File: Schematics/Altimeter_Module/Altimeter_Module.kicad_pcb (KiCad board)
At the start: 4 copper layers, 69.5 x 60 mm, 104 parts, among them J1 Stack Male Edge Connector, J2 Main E-Match, J3 Drogue E-Match, J4 USB_B_Micro, J5 SWD_01x04_Pin, Q1 AO3400A, Q2 AO4406AL, Q3 AO3400A, Q4 AO3400A, Q5 AO4406AL, SW1 SW_STM_RESET, SW2 SW_STM_BOOT_MODE, U1 KX134-1211, U10 ACS70331EOLC, U12 AMS1117-3.3, U2 MS560702BA03-50, U3 W25Q128JVS, U4 LM66100DCKR, U5 LM66100DCKR, U6 STM32F103CBT6, U7 LM66100DCKR, U8 ISO1042BDWVR, U9 MPU-6050, Y1 X322516MMB4SI

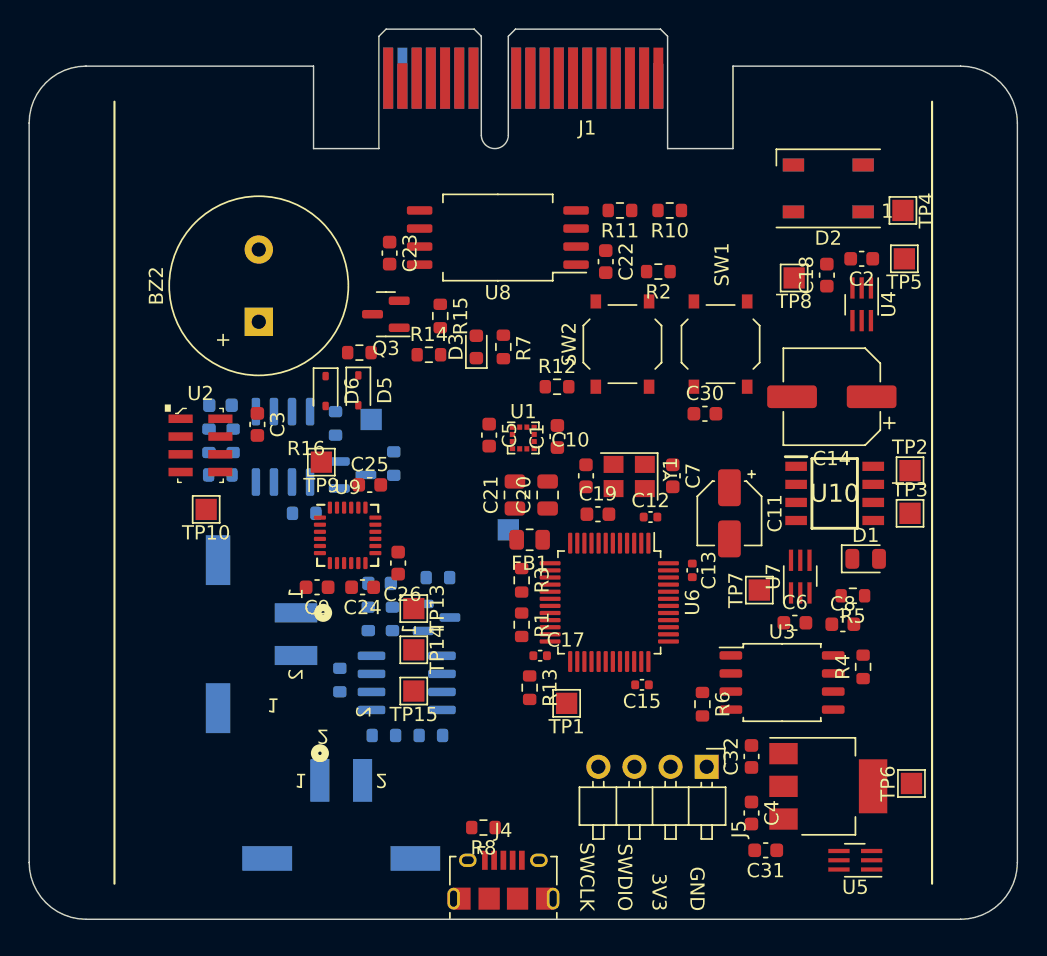
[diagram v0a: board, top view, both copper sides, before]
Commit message: Reset PCB layout
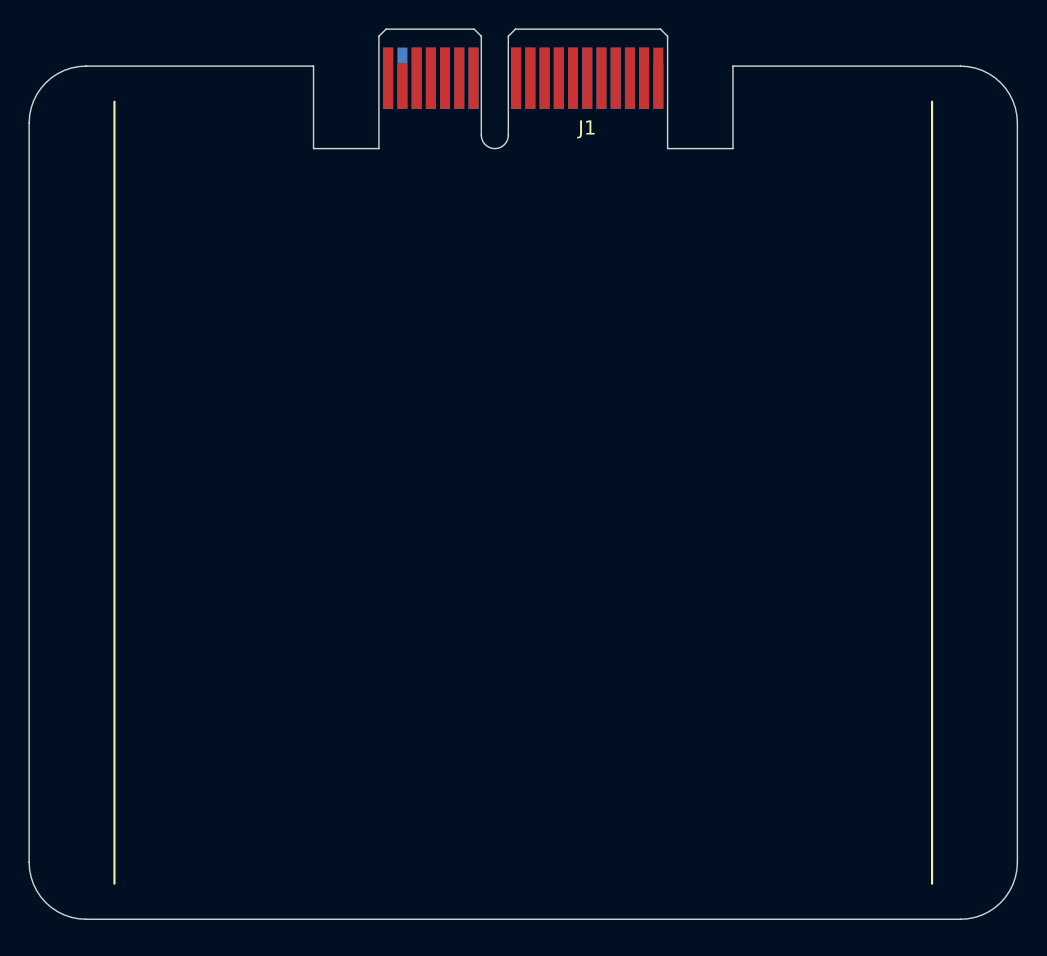
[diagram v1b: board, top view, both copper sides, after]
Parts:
- removed BZ2: PKM13EPYH4000, footprints:Buzzer_12.6x9.5RM5.0
- removed C1, C24, C3, C30, C5, C8, C9: 100nF, Capacitor_SMD:C_0603_1608Metric
- removed C10, C7: 10p, Capacitor_SMD:C_0603_1608Metric
- removed C11: 10uF, Capacitor_SMD:CP_Elec_4x5.4
- removed C12, C13, C15, C17: 100n, Capacitor_SMD:C_0402_1005Metric
- removed C14: 100uF, Capacitor_SMD:CP_Elec_6.3x5.9
- removed C18: 0.1uF, Capacitor_SMD:C_0603_1608Metric
- removed C19: 10n, Capacitor_SMD:C_0603_1608Metric
- removed C2, C4, C6: 1uF, Capacitor_SMD:C_0603_1608Metric
- removed C20, C21: 1uF, Capacitor_SMD:C_0805_2012Metric
- removed C22, C23: 0.1u, Capacitor_SMD:C_0603_1608Metric
- removed C25: 2.2nF, Capacitor_SMD:C_0603_1608Metric
- removed C26: 10nF, Capacitor_SMD:C_0603_1608Metric
- removed C31, C32: 10uF, Capacitor_SMD:C_0603_1608Metric
- removed D1: PWR_LED (GRN), LED_SMD:LED_0805_2012Metric
- removed D2, D4: WS2812B, LED_SMD:LED_WS2812B_PLCC4_5.0x5.0mm_P3.2mm
- removed D3: DB_LED (YLW), LED_SMD:LED_0603_1608Metric
- removed D5, D6: 1N5819WS, Diode_SMD:D_SOD-323
- removed D7: FIRE_MAIN (RED), LED_SMD:LED_0603_1608Metric
- removed D8: FIRE_DRGE (RED), LED_SMD:LED_0603_1608Metric
- removed FB1: 100R, Resistor_SMD:R_0805_2012Metric
- removed J2: Main E-Match, footprints:CONN_2-1445057-2_TYCO
- removed J3: Drogue E-Match, footprints:CONN_2-1445057-2_TYCO
- removed J4: USB_B_Micro, footprints:USB_Micro-B_Amphenol_10118194_Horizontal
- removed J5: SWD_01x04_Pin, SWD_Header:SWD_PinHeader_1x04_P2.54mm_Horizontal
- removed Q1, Q3, Q4: AO3400A, Package_TO_SOT_SMD:SOT-23
- removed Q2, Q5: AO4406AL, Package_SO:SOIC-8_3.9x4.9mm_P1.27mm
- removed R1, R3: 4.7k, Resistor_SMD:R_0603_1608Metric
- removed R10: 30k, Resistor_SMD:R_0603_1608Metric
- removed R11, R15, R19, R2, R25, R4, R6: 10k, Resistor_SMD:R_0603_1608Metric
- removed R12, R13, R17, R21, R22, R23: 100k, Resistor_SMD:R_0603_1608Metric
- removed R14, R18, R20, R24, R26, R27, R9: 510R, Resistor_SMD:R_0603_1608Metric
- removed R16: 1k, Resistor_SMD:R_0603_1608Metric
- removed R5: 820R, Resistor_SMD:R_0603_1608Metric
- removed R7: 560R, Resistor_SMD:R_0603_1608Metric
- removed R8: 1.5k, Resistor_SMD:R_0603_1608Metric
- removed SW1: SW_STM_RESET, Button_Switch_SMD:SW_Push_1P1T_XKB_TS-1187A
- removed SW2: SW_STM_BOOT_MODE, Button_Switch_SMD:SW_Push_1P1T_XKB_TS-1187A
- removed TP1: TP_BSENSE, TestPoint:TestPoint_Pad_1.5x1.5mm
- removed TP10: TP_SCL, TestPoint:TestPoint_Pad_1.5x1.5mm
- removed TP11: TP_CMAIN, TestPoint:TestPoint_Pad_1.5x1.5mm
- removed TP12: TP_CDRGE, TestPoint:TestPoint_Pad_1.5x1.5mm
- removed TP13: TP_PA5, TestPoint:TestPoint_Pad_1.5x1.5mm
- removed TP14: TP_PA6, TestPoint:TestPoint_Pad_1.5x1.5mm
- removed TP15: TP_PA7, TestPoint:TestPoint_Pad_1.5x1.5mm
- removed TP2: TP_ISENSE, TestPoint:TestPoint_Pad_1.5x1.5mm
- removed TP3: TP_GND, TestPoint:TestPoint_Pad_1.5x1.5mm
- removed TP4: TP_3V3, TestPoint:TestPoint_Pad_1.5x1.5mm
- removed TP5: TP_VSTACK, TestPoint:TestPoint_Pad_1.5x1.5mm
- removed TP6: TP_VUSB, TestPoint:TestPoint_Pad_1.5x1.5mm
- removed TP7: TP_VSWD, TestPoint:TestPoint_Pad_1.5x1.5mm
- removed TP8: TP_MUX, TestPoint:TestPoint_Pad_1.5x1.5mm
- removed TP9: TP_SDA, TestPoint:TestPoint_Pad_1.5x1.5mm
- removed U1: KX134-1211, Package_LGA:LGA-12_2x2mm_P0.5mm
- removed U10: ACS70331EOLC, footprints:SOIC127P600X175-8N
- removed U12: AMS1117-3.3, Package_TO_SOT_SMD:SOT-223-3_TabPin2
- removed U2: MS560702BA03-50, footprints:MS5607_Handsolder
- removed U3: W25Q128JVS, Package_SO:SOIC-8_5.23x5.23mm_P1.27mm
- removed U4, U5, U7: LM66100DCKR, LMR66100:SC-70-6_Handsoldering
- removed U6: STM32F103CBT6, Package_QFP:LQFP-48_7x7mm_P0.5mm
- removed U8: ISO1042BDWVR, ISO1042:SOIC-8 ISO1042BDWV
- removed U9: MPU-6050, Sensor_Motion:InvenSense_QFN-24_4x4mm_P0.5mm
- removed Y1: X322516MMB4SI, Crystal:Crystal_SMD_3225-4Pin_3.2x2.5mm
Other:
- board text removed: "Find way to place e-match parts"

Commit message: Preliminary PCB layout (DRC passes)
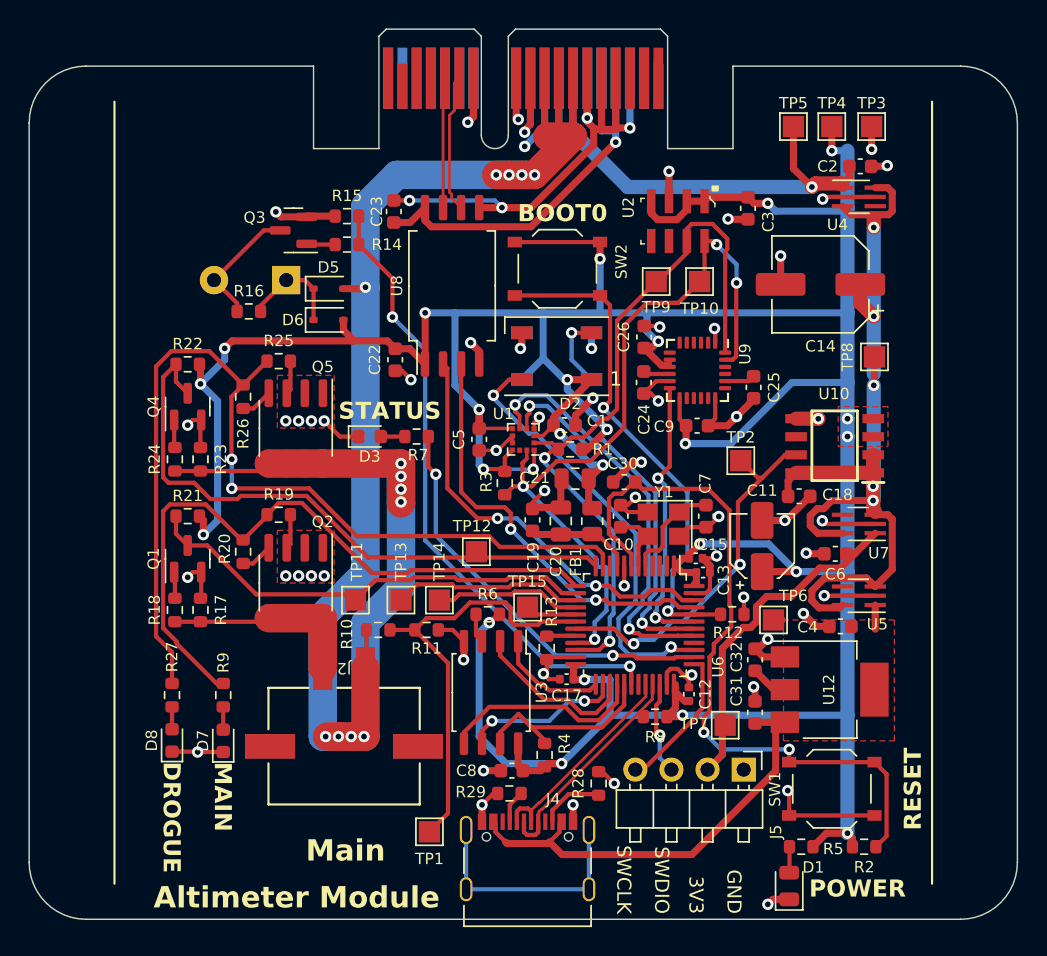
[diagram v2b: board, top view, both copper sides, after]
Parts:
- added BZ2: PKM13EPYH4000, footprints:Buzzer_12.6x9.5RM5.0, B.Cu at (130.9, 72.5)
- added C1: 100nF, Capacitor_SMD:C_0603_1608Metric, F.Cu at (149.2, 82.7)
- added C10: 10p, Capacitor_SMD:C_0603_1608Metric, F.Cu at (153.2, 89.1)
- added C11: 10uF, Capacitor_SMD:CP_Elec_4x5.4, F.Cu at (163.1, 91.2)
- added C12: 100n, Capacitor_SMD:C_0402_1005Metric, F.Cu at (157.9, 101.6)
- added C13: 100n, Capacitor_SMD:C_0402_1005Metric, F.Cu at (158.9, 93.1)
- added C14: 100uF, Capacitor_SMD:CP_Elec_6.3x5.9, F.Cu at (167.2, 72.8)
- added C15: 100n, Capacitor_SMD:C_0402_1005Metric, F.Cu at (158.4, 92.1)
- added C17: 100n, Capacitor_SMD:C_0402_1005Metric, F.Cu at (149.3, 100.6)
- added C18: 0.1uF, Capacitor_SMD:C_0603_1608Metric, F.Cu at (165.7, 87.7)
- added C19: 10n, Capacitor_SMD:C_0603_1608Metric, F.Cu at (146.9, 89.4)
- added C2: 1uF, Capacitor_SMD:C_0603_1608Metric, F.Cu at (170.0, 64.5)
- added C20: 1uF, Capacitor_SMD:C_0805_2012Metric, F.Cu at (148.9, 89.4)
- added C21: 1uF, Capacitor_SMD:C_0805_2012Metric, F.Cu at (149.9, 86.5)
- added C22: 0.1u, Capacitor_SMD:C_0603_1608Metric, F.Cu at (137.3, 78.1)
- added C23: 0.1u, Capacitor_SMD:C_0603_1608Metric, F.Cu at (137.2, 67.7)
- added C24: 100nF, Capacitor_SMD:C_0603_1608Metric, F.Cu at (154.8, 79.7)
- added C25: 2.2nF, Capacitor_SMD:C_0603_1608Metric, F.Cu at (162.5, 80.0)
- added C26: 10nF, Capacitor_SMD:C_0603_1608Metric, F.Cu at (154.8, 76.5)
- added C3: 100nF, Capacitor_SMD:C_0603_1608Metric, F.Cu at (162.1, 67.5)
- added C30: 100nF, Capacitor_SMD:C_0603_1608Metric, F.Cu at (153.4, 86.7)
- added C31: 10uF, Capacitor_SMD:C_0603_1608Metric, F.Cu at (162.6, 102.9)
- added C32: 10uF, Capacitor_SMD:C_0603_1608Metric, F.Cu at (162.6, 99.2)
- added C4: 1uF, Capacitor_SMD:C_0603_1608Metric, F.Cu at (168.6, 96.8)
- added C5: 100nF, Capacitor_SMD:C_0603_1608Metric, F.Cu at (143.2, 83.7)
- added C6: 1uF, Capacitor_SMD:C_0603_1608Metric, F.Cu at (168.2, 91.8)
- added C7: 10p, Capacitor_SMD:C_0603_1608Metric, F.Cu at (159.2, 89.1)
- added C8: 100nF, Capacitor_SMD:C_0603_1608Metric, F.Cu at (145.5, 107.0)
- added C9: 100nF, Capacitor_SMD:C_0603_1608Metric, F.Cu at (158.5, 82.7)
- added D1: PWR_LED (GRN), LED_SMD:LED_0805_2012Metric, F.Cu at (165.0, 115.1)
- added D2: WS2812B, LED_SMD:LED_WS2812B_PLCC4_5.0x5.0mm_P3.2mm, F.Cu at (148.7, 77.8)
- added D3: DB_LED (YLW), LED_SMD:LED_0603_1608Metric, F.Cu at (135.5, 83.5)
- added D4: WS2812B, LED_SMD:LED_WS2812B_PLCC4_5.0x5.0mm_P3.2mm, B.Cu at (148.7, 77.8)
- added D5: 1N5819WS, Diode_SMD:D_SOD-323, F.Cu at (132.6, 73.1)
- added D6: 1N5819WS, Diode_SMD:D_SOD-323, F.Cu at (132.6, 75.3)
- added D7: FIRE_MAIN (RED), LED_SMD:LED_0603_1608Metric, F.Cu at (125.2, 104.9)
- added D8: FIRE_DRGE (RED), LED_SMD:LED_0603_1608Metric, F.Cu at (121.6, 104.9)
- added FB1: 100R, Resistor_SMD:R_0805_2012Metric, F.Cu at (151.2, 89.5)
- added J2: Main E-Match, footprints:CONN_2-1445057-2_TYCO, F.Cu at (135.2, 99.8)
- added J3: Drogue E-Match, footprints:CONN_2-1445057-2_TYCO, B.Cu at (132.2, 99.8)
- added J4: USB_C_Female_USB2_Small, footprints:USB_C_DB-108PWB, F.Cu at (146.6, 113.1)
- added J5: SWD_01x04_Pin, SWD_Header:SWD_PinHeader_1x04_P2.54mm_Horizontal, F.Cu at (161.8, 106.9)
- added Q1: AO3400A, Package_TO_SOT_SMD:SOT-23, F.Cu at (122.7, 92.1)
- added Q2: AO4406AL, Package_SO:SOIC-8_3.9x4.9mm_P1.27mm, F.Cu at (130.3, 93.8)
- added Q3: AO3400A, Package_TO_SOT_SMD:SOT-23, F.Cu at (130.1, 69.0)
- added Q4: AO3400A, Package_TO_SOT_SMD:SOT-23, F.Cu at (122.7, 81.4)
- added Q5: AO4406AL, Package_SO:SOIC-8_3.9x4.9mm_P1.27mm, F.Cu at (130.3, 82.9)
- added R1: 4.7k, Resistor_SMD:R_0603_1608Metric, F.Cu at (149.6, 84.4)
- added R10: 30k, Resistor_SMD:R_0603_1608Metric, F.Cu at (136.1, 97.1)
- added R11: 10k, Resistor_SMD:R_0603_1608Metric, F.Cu at (139.5, 97.1)
- added R12: 100k, Resistor_SMD:R_0603_1608Metric, F.Cu at (161.0, 96.0)
- added R13: 100k, Resistor_SMD:R_0603_1608Metric, F.Cu at (147.9, 98.4)
- added R14: 510R, Resistor_SMD:R_0603_1608Metric, F.Cu at (133.9, 70.0)
- added R15: 10k, Resistor_SMD:R_0603_1608Metric, F.Cu at (133.9, 68.0)
- added R16: 1k, Resistor_SMD:R_0603_1608Metric, F.Cu at (127.0, 74.7)
- added R17: 100k, Resistor_SMD:R_0603_1608Metric, F.Cu at (123.6, 95.7)
- added R18: 510R, Resistor_SMD:R_0603_1608Metric, F.Cu at (121.8, 95.7)
- added R19: 10k, Resistor_SMD:R_0603_1608Metric, F.Cu at (129.1, 89.0)
- added R2: 10k, Resistor_SMD:R_0603_1608Metric, F.Cu at (170.3, 112.3)
- added R20: 510R, Resistor_SMD:R_0603_1608Metric, F.Cu at (126.6, 91.6)
- added R21: 100k, Resistor_SMD:R_0603_1608Metric, F.Cu at (122.7, 89.1)
- added R22: 100k, Resistor_SMD:R_0603_1608Metric, F.Cu at (122.7, 78.4)
- added R23: 100k, Resistor_SMD:R_0603_1608Metric, F.Cu at (123.6, 85.1)
- added R24: 510R, Resistor_SMD:R_0603_1608Metric, F.Cu at (121.8, 85.1)
- added R25: 10k, Resistor_SMD:R_0603_1608Metric, F.Cu at (129.1, 78.2)
- added R26: 510R, Resistor_SMD:R_0603_1608Metric, F.Cu at (126.6, 80.7)
- added R27: 510R, Resistor_SMD:R_0603_1608Metric, F.Cu at (121.6, 101.7)
- added R28: 5.1k, Resistor_SMD:R_0603_1608Metric, F.Cu at (151.6, 107.9)
- added R29: 5.1k, Resistor_SMD:R_0603_1608Metric, F.Cu at (145.3, 108.6)
- added R3: 4.7k, Resistor_SMD:R_0603_1608Metric, F.Cu at (145.0, 86.8)
- added R4: 10k, Resistor_SMD:R_0603_1608Metric, F.Cu at (147.8, 105.9)
- added R5: 820R, Resistor_SMD:R_0603_1608Metric, F.Cu at (165.8, 112.3)
- added R6: 10k, Resistor_SMD:R_0603_1608Metric, F.Cu at (143.8, 96.0)
- added R7: 560R, Resistor_SMD:R_0603_1608Metric, F.Cu at (138.8, 83.5)
- added R8: 1.5k, Resistor_SMD:R_0603_1608Metric, F.Cu at (155.6, 103.2)
- added R9: 510R, Resistor_SMD:R_0603_1608Metric, F.Cu at (125.2, 101.7)
- added SW1: SW_STM_RESET, Button_Switch_SMD:SW_Push_1P1T_XKB_TS-1187A, F.Cu at (168.0, 108.3)
- added SW2: SW_STM_BOOT_MODE, Button_Switch_SMD:SW_Push_1P1T_XKB_TS-1187A, F.Cu at (148.7, 71.7)
- added TP1: TP_BSENSE, TestPoint:TestPoint_Pad_1.5x1.5mm, F.Cu at (139.7, 111.3)
- added TP10: TP_SCL, TestPoint:TestPoint_Pad_1.5x1.5mm, F.Cu at (158.7, 72.6)
- added TP11: TP_CMAIN, TestPoint:TestPoint_Pad_1.5x1.5mm, F.Cu at (134.5, 95.0)
- added TP12: TP_CDRGE, TestPoint:TestPoint_Pad_1.5x1.5mm, F.Cu at (143.0, 91.6)
- added TP13: TP_PA5, TestPoint:TestPoint_Pad_1.5x1.5mm, F.Cu at (137.7, 95.0)
- added TP14: TP_PA6, TestPoint:TestPoint_Pad_1.5x1.5mm, F.Cu at (140.4, 95.0)
- added TP15: TP_PA7, TestPoint:TestPoint_Pad_1.5x1.5mm, F.Cu at (146.6, 95.5)
- added TP2: TP_ISENSE, TestPoint:TestPoint_Pad_1.5x1.5mm, F.Cu at (161.6, 85.2)
- added TP3: TP_GND, TestPoint:TestPoint_Pad_1.5x1.5mm, F.Cu at (170.8, 61.7)
- added TP4: TP_3V3, TestPoint:TestPoint_Pad_1.5x1.5mm, F.Cu at (168.0, 61.7)
- added TP5: TP_VSTACK, TestPoint:TestPoint_Pad_1.5x1.5mm, F.Cu at (165.3, 61.7)
- added TP6: TP_VUSB, TestPoint:TestPoint_Pad_1.5x1.5mm, F.Cu at (163.9, 96.4)
- added TP7: TP_VSWD, TestPoint:TestPoint_Pad_1.5x1.5mm, F.Cu at (160.5, 103.8)
- added TP8: TP_MUX, TestPoint:TestPoint_Pad_1.5x1.5mm, F.Cu at (171.0, 77.9)
- added TP9: TP_SDA, TestPoint:TestPoint_Pad_1.5x1.5mm, F.Cu at (155.7, 72.6)
- added U1: KX134-1211, Package_LGA:LGA-12_2x2mm_P0.5mm, F.Cu at (146.3, 83.7)
- added U10: ACS70331EOLC, footprints:SOIC127P600X175-8N, F.Cu at (168.2, 84.2)
- added U12: AMS1117-3.3, Package_TO_SOT_SMD:SOT-223-3_TabPin2, F.Cu at (167.8, 101.3)
- added U2: MS560702BA03-50, footprints:MS5607_Handsolder, F.Cu at (157.2, 68.3)
- added U3: W25Q128JVS, Package_SO:SOIC-8_5.23x5.23mm_P1.27mm, F.Cu at (144.0, 101.5)
- added U4: LM66100DCKR, LMR66100:SC-70-6_Handsoldering, F.Cu at (169.9, 66.7)
- added U5: LM66100DCKR, LMR66100:SC-70-6_Handsoldering, F.Cu at (169.9, 94.7)
- added U6: STM32F103CBT6, Package_QFP:LQFP-48_7x7mm_P0.5mm, F.Cu at (154.2, 96.8)
- added U7: LM66100DCKR, LMR66100:SC-70-6_Handsoldering, F.Cu at (169.9, 89.7)
- added U8: ISO1042BDWVR, ISO1042:SOIC-8 ISO1042BDWV, F.Cu at (141.3, 72.9)
- added U9: MPU-6050, Sensor_Motion:InvenSense_QFN-24_4x4mm_P0.5mm, F.Cu at (158.6, 78.8)
- added Y1: X322516MMB4SI, Crystal:Crystal_SMD_3225-4Pin_3.2x2.5mm, F.Cu at (156.2, 89.7)
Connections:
- J1 pad A13: DB_LED -> unconnected-(J1-DB_LED-PadA13)
- J1 pad A3: unconnected-(J1-GND_A-PadA3) -> GND2
- J1 pad A6: unconnected-(J1-GND_A-PadA3) -> GND2
- J1 pad B4: unconnected-(J1-GND_A-PadA3) -> GND2
- J1 pad B5: unconnected-(J1-GND_A-PadA3) -> GND2
- J1 pad B6: unconnected-(J1-GND_A-PadA3) -> GND2
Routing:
- net +3.3V: track 0.00 -> 297.6 mm, vias 0 -> 25
- net GND: track 0.00 -> 146.5 mm, vias 0 -> 57
- net +BATT: track 0.00 -> 86.4 mm, vias 0 -> 9
- net FIRE_DRGE: track 0.00 -> 69.2 mm, vias 0 -> 2
- net V_MUX: track 0.00 -> 64.2 mm, vias 0 -> 5
- net SCL: track 0.00 -> 54.9 mm, vias 0 -> 4
- net SDA: track 0.00 -> 52.1 mm, vias 0 -> 2
- net STM_RESET: track 0.00 -> 51.6 mm, vias 0 -> 2
- net FIRE_MAIN: track 0.00 -> 47.9 mm
- net BUZZER: track 0.00 -> 44.1 mm, vias 0 -> 2
- net CONTINUITY_DRGE: track 0.00 -> 43.9 mm
- net GND2: track 0.00 -> 38.7 mm, vias 0 -> 4
- net V_PSU: track 0.00 -> 35.6 mm, vias 0 -> 1
- net BOOT0: track 0.00 -> 35.5 mm, vias 0 -> 2
- net Net-(J3-Pad2): track 0.00 -> 34.4 mm, vias 0 -> 4
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- added copper zone on F.Cu, net +3.3V
- added copper zone on F.Cu, net GND
- added copper zone on In1.Cu, net GND
- added copper zone on In2.Cu, net GND
- added copper zone on F.Cu, net V_REGUSB
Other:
- board text added: "-Pin1 Dots -XYZ arrows"
- board text added: "Altimeter Module"
- board text added: "BOOT0"
- board text added: "DROGUE"
- board text added: "Drogue"
- board text added: "MAIN"
- board text added: "Main"
- board text added: "POWER"
- board text added: "Q-AIMS V1 QRET Avionics Interconnected Module Standard"
- board text added: "RESET"
- board text added: "STATUS"
- board text removed: "check communications module for examples"

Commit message: Silkscreen adjustments
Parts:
- renumbered BZ2 to BZ1
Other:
- board text added: "+X"
- board text added: "+Y"
- board text added: "+Z"
- board text added: "A.I.M Standard (1st Gen)"
- board text added: "OKA"
- board text added: "Oka Rev 1.0 QRET Mar 2024 Joshua Xiang Kennan Bays"
- board text added: "Secondary Module"
- board text removed: "-Pin1 Dots -XYZ arrows"
- board text removed: "Q-AIMS V1 QRET Avionics Interconnected Module Standard"

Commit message: Adjusted power/debug LED resistors & small BoM tweaks
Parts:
- R5: value 820R -> 1.2k
- R7: value 560R -> 680R
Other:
- board text removed: "PLACE USB, SWD, E-MATCH CONNECTORS HERE (okay if e-match on bottom)"
